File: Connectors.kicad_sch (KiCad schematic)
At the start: 4 parts, among them J1 Conn_01x04_Pin, J2 Conn_01x04_Pin, J3 Conn_01x09_Pin, J4 Conn_02x03_Odd_Even

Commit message: Completed symbol to footprint association
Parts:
- J1, J2: footprint (none) -> Connector_PinHeader_2.54mm:PinHeader_1x04_P2.54mm_Vertical
- J3: footprint (none) -> Connector_PinHeader_2.54mm:PinHeader_1x09_P2.54mm_Vertical
- J4: footprint (none) -> Connector_PinHeader_2.54mm:PinHeader_2x03_P2.54mm_Vertical
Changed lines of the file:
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@@
 			)
 		)
-		(property "Footprint" ""
+		(property "Footprint" "Connector_PinHeader_2.54mm:PinHeader_2x03_P2.54mm_Vertical"
 			(at 63.5 67.31 0)
 			(hide yes)
@@
 			)
 		)
-		(property "Footprint" ""
+		(property "Footprint" "Connector_PinHeader_2.54mm:PinHeader_1x04_P2.54mm_Vertical"
 			(at 33.02 40.64 0)
 			(hide yes)
@@
 			)
 		)
-		(property "Footprint" ""
+		(property "Footprint" "Connector_PinHeader_2.54mm:PinHeader_1x04_P2.54mm_Vertical"
 			(at 62.23 41.91 0)
 			(hide yes)
@@
 			)
 		)
-		(property "Footprint" ""
+		(property "Footprint" "Connector_PinHeader_2.54mm:PinHeader_1x09_P2.54mm_Vertical"
 			(at 34.29 71.12 0)
 			(hide yes)

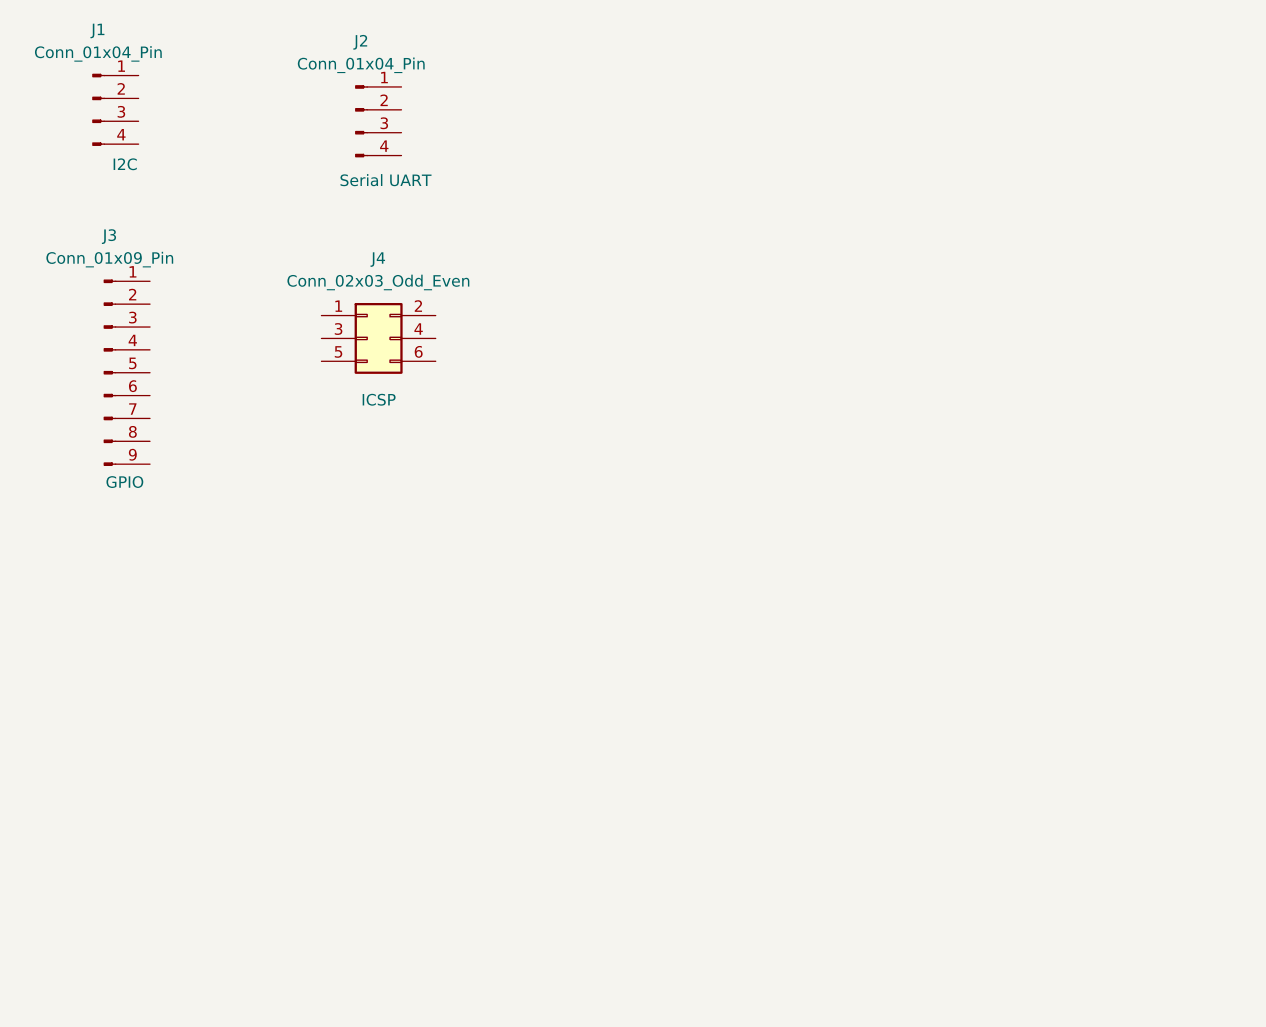
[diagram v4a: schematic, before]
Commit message: Updated wiring of both sheets
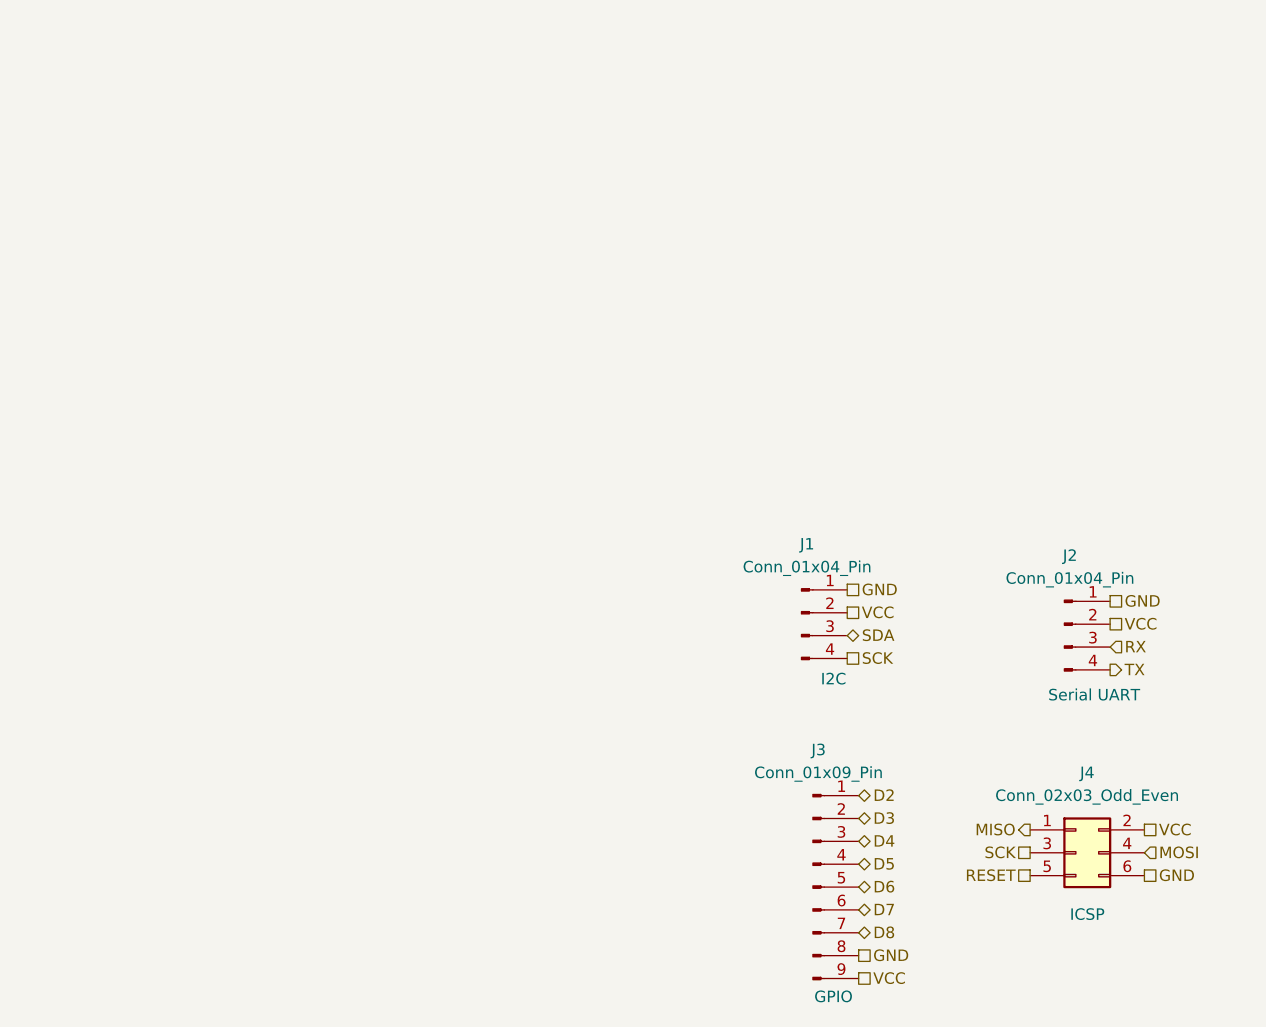
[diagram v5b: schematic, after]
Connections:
- net MISO: now reaches J4.1 (Pin_1)
- net VCC: now reaches J4.2 (Pin_2)
- net VCC: now also J1.2 (Pin_2), J2.2 (Pin_2), J3.9 (Pin_9)
- net SCK: now reaches J4.3 (Pin_3)
- net SCK: now also J1.4 (Pin_4)
- net MOSI: now reaches J4.4 (Pin_4)
- net RESET: now reaches J4.5 (Pin_5)
- net GND: now reaches J4.6 (Pin_6)
- net GND: now also J1.1 (Pin_1), J2.1 (Pin_1), J3.8 (Pin_8)
- net SDA: now reaches J1.3 (Pin_3)
- net RX: now reaches J2.3 (Pin_3)
- net TX: now reaches J2.4 (Pin_4)
- net D2: now reaches J3.1 (Pin_1)
- net D3: now reaches J3.2 (Pin_2)
- net D4: now reaches J3.3 (Pin_3)
- net D5: now reaches J3.4 (Pin_4)
- net D6: now reaches J3.5 (Pin_5)
- net D7: now reaches J3.6 (Pin_6)
- net D8: now reaches J3.7 (Pin_7)
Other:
- moved on the sheet: J1, J2, J3, J4

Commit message: Completed comments
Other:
- moved on the sheet: J1, J2, J4
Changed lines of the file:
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@@
 	(hierarchical_label "SDA"
 		(shape bidirectional)
-		(at 116.84 100.33 0)
+		(at 116.84 97.79 0)
 		(effects
 			(font
@@
 	(hierarchical_label "RX"
 		(shape input)
-		(at 146.05 101.6 0)
+		(at 146.05 97.79 0)
 		(effects
 			(font
@@
 	(hierarchical_label "GND"
 		(shape passive)
+		(at 116.84 92.71 0)
+		(effects
+			(font
+				(size 1.27 1.27)
+			)
+			(justify left)
+		)
+	)
+	(hierarchical_label "D7"
+		(shape bidirectional)
+		(at 118.11 130.81 0)
+		(effects
+			(font
+				(size 1.27 1.27)
+			)
+			(justify left)
+		)
+	)
+	(hierarchical_label "D2"
+		(shape bidirectional)
+		(at 118.11 118.11 0)
+		(effects
+			(font
+				(size 1.27 1.27)
+			)
+			(justify left)
+		)
+	)
+	(hierarchical_label "D5"
+		(shape bidirectional)
+		(at 118.11 125.73 0)
+		(effects
+			(font
+				(size 1.27 1.27)
+			)
+			(justify left)
+		)
+	)
+	(hierarchical_label "VCC"
+		(shape passive)
 		(at 116.84 95.25 0)
-		(effects
-			(font
-				(size 1.27 1.27)
-			)
-			(justify left)
-		)
-	)
-	(hierarchical_label "D7"
-		(shape bidirectional)
-		(at 118.11 130.81 0)
-		(effects
-			(font
-				(size 1.27 1.27)
-			)
-			(justify left)
-		)
-	)
-	(hierarchical_label "D2"
-		(shape bidirectional)
-		(at 118.11 118.11 0)
-		(effects
-			(font
-				(size 1.27 1.27)
-			)
-			(justify left)
-		)
-	)
-	(hierarchical_label "D5"
-		(shape bidirectional)
-		(at 118.11 125.73 0)
-		(effects
-			(font
-				(size 1.27 1.27)
-			)
-			(justify left)
-		)
-	)
-	(hierarchical_label "VCC"
-		(shape passive)
-		(at 116.84 97.79 0)
 		(effects
 			(font
@@
 	(hierarchical_label "MISO"
 		(shape output)
-		(at 137.16 121.92 180)
+		(at 140.97 119.38 180)
 		(effects
 			(font
@@
 	(hierarchical_label "MOSI"
 		(shape input)
-		(at 149.86 124.46 0)
+		(at 153.67 121.92 0)
 		(effects
 			(font
@@
 	(hierarchical_label "VCC"
 		(shape passive)
-		(at 146.05 99.06 0)
+		(at 146.05 95.25 0)
 		(effects
 			(font
@@
 	(hierarchical_label "SCK"
 		(shape passive)
-		(at 116.84 102.87 0)
+		(at 116.84 100.33 0)
 		(effects
 			(font
@@
 	(hierarchical_label "GND"
 		(shape passive)
-		(at 146.05 96.52 0)
+		(at 146.05 92.71 0)
 		(effects
 			(font
@@
 	(hierarchical_label "VCC"
 		(shape passive)
-		(at 149.86 121.92 0)
+		(at 153.67 119.38 0)
 		(effects
 			(font
@@
 	(hierarchical_label "RESET"
 		(shape passive)
-		(at 137.16 127 180)
+		(at 140.97 124.46 180)
 		(effects
 			(font
@@
 	(hierarchical_label "TX"
 		(shape output)
-		(at 146.05 104.14 0)
+		(at 146.05 100.33 0)
 		(effects
 			(font
@@
 	(hierarchical_label "GND"
 		(shape passive)
-		(at 149.86 127 0)
+		(at 153.67 124.46 0)
 		(effects
 			(font
@@
 	(hierarchical_label "SCK"
 		(shape passive)
-		(at 137.16 124.46 180)
+		(at 140.97 121.92 180)
 		(effects
 			(font
@@
 	(symbol
 		(lib_id "Connector_Generic:Conn_02x03_Odd_Even")
-		(at 142.24 124.46 0)
+		(at 146.05 121.92 0)
 		(unit 1)
 		(body_style 1)
@@
 		(dnp no)
 		(property "Reference" "J4"
-			(at 143.51 115.57 0)
+			(at 147.32 113.03 0)
 			(show_name no)
 			(do_not_autoplace no)
@@
 		)
 		(property "Value" "Conn_02x03_Odd_Even"
-			(at 143.51 118.11 0)
+			(at 147.32 115.57 0)
 			(show_name no)
 			(do_not_autoplace no)
@@
 		)
 		(property "Footprint" "Connector_PinHeader_2.54mm:PinHeader_2x03_P2.54mm_Vertical"
-			(at 142.24 124.46 0)
+			(at 146.05 121.92 0)
 			(hide yes)
 			(show_name no)
@@
 		)
 		(property "Datasheet" ""
-			(at 142.24 124.46 0)
+			(at 146.05 121.92 0)
 			(hide yes)
 			(show_name no)
@@
 		)
 		(property "Description" "Generic connector, double row, 02x03, odd/even pin numbering scheme (row 1 odd numbers, row 2 even numbers), script generated (kicad-library-utils/schlib/autogen/connector/)"
-			(at 142.24 124.46 0)
+			(at 146.05 121.92 0)
 			(hide yes)
 			(show_name no)
@@
 		)
 		(property "Purpose" "ICSP"
-			(at 143.51 131.318 0)
+			(at 147.32 128.778 0)
 			(show_name no)
 			(do_not_autoplace no)
@@
 	(symbol
 		(lib_id "Connector:Conn_01x04_Pin")
-		(at 111.76 97.79 0)
+		(at 111.76 95.25 0)
 		(unit 1)
 		(body_style 1)
@@
 		(dnp no)
 		(property "Reference" "J1"
+			(at 112.395 87.63 0)
+			(show_name no)
+			(do_not_autoplace no)
+			(effects
+				(font
+					(size 1.27 1.27)
+				)
+			)
+		)
+		(property "Value" "Conn_01x04_Pin"
 			(at 112.395 90.17 0)
 			(show_name no)
@@
 			)
 		)
-		(property "Value" "Conn_01x04_Pin"
-			(at 112.395 92.71 0)
-			(show_name no)
-			(do_not_autoplace no)
-			(effects
-				(font
-					(size 1.27 1.27)
-				)
-			)
-		)
 		(property "Footprint" "Connector_PinHeader_2.54mm:PinHeader_1x04_P2.54mm_Vertical"
-			(at 111.76 97.79 0)
+			(at 111.76 95.25 0)
 			(hide yes)
 			(show_name yes)
@@
 		)
 		(property "Datasheet" ""
-			(at 111.76 97.79 0)
+			(at 111.76 95.25 0)
 			(hide yes)
 			(show_name no)
@@
 		)
 		(property "Description" "Generic connector, single row, 01x04, script generated"
-			(at 111.76 97.79 0)
+			(at 111.76 95.25 0)
 			(hide yes)
 			(show_name no)
@@
 		)
 		(property "Purpose" "I2C"
-			(at 115.316 105.156 0)
+			(at 115.316 102.616 0)
 			(show_name no)
 			(do_not_autoplace no)
@@
 	(symbol
 		(lib_id "Connector:Conn_01x04_Pin")
-		(at 140.97 99.06 0)
+		(at 140.97 95.25 0)
 		(unit 1)
 		(body_style 1)
@@
 		(dnp no)
 		(property "Reference" "J2"
-			(at 141.605 91.44 0)
+			(at 141.605 87.63 0)
 			(show_name no)
 			(do_not_autoplace no)
@@
 		)
 		(property "Value" "Conn_01x04_Pin"
-			(at 141.605 93.98 0)
+			(at 141.605 90.17 0)
 			(show_name no)
 			(do_not_autoplace no)
@@
 		)
 		(property "Footprint" "Connector_PinHeader_2.54mm:PinHeader_1x04_P2.54mm_Vertical"
-			(at 140.97 99.06 0)
+			(at 140.97 95.25 0)
 			(hide yes)
 			(show_name yes)
@@
 		)
 		(property "Datasheet" ""
-			(at 140.97 99.06 0)
+			(at 140.97 95.25 0)
 			(hide yes)
 			(show_name no)
@@
 		)
 		(property "Description" "Generic connector, single row, 01x04, script generated"
-			(at 140.97 99.06 0)
+			(at 140.97 95.25 0)
 			(hide yes)
 			(show_name no)
@@
 		)
 		(property "Purpose" "Serial UART"
-			(at 144.272 106.934 0)
-			(show_name no)
-			(do_not_autoplace no)
+			(at 144.272 103.124 0)
+			(show_name no)
+			(do_not_autoplace no)
